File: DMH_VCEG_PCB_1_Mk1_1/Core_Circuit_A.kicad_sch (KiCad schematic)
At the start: 112 parts, among them J21 Conn_01x10_PinHeader, J22 Conn_01x10_PinHeader, J23 Conn_01x10_PinHeader, J24 Conn_01x06_PinHeader, Q1 BC558, Q10 BC548, Q2 BC558, Q3 BC548, Q4 BC548, Q5 BS170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

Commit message: Out R rework ongoing
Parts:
- removed Q5, Q6: BS170, Package_TO_SOT_THT:TO-92_Inline, symbol Transistor_FET:BS170
- R8: value 100k -> 150k
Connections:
- net +12V: now also Q2.3 (E), R1.1
- net -12V: no longer RV2.1, RV2.2
- net GND: no longer U7.12 (+)
- net InvGate: no longer R3.1
- net at R6.1: no longer RV2.3
- now unconnected: R3.2, R6.2, RV1.1, RV1.2, RV1.3, U7.13 (-), U7.14
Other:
- moved on the sheet: Q1, Q2, R1, R3, R6, R8, RV1, RV2, U7D

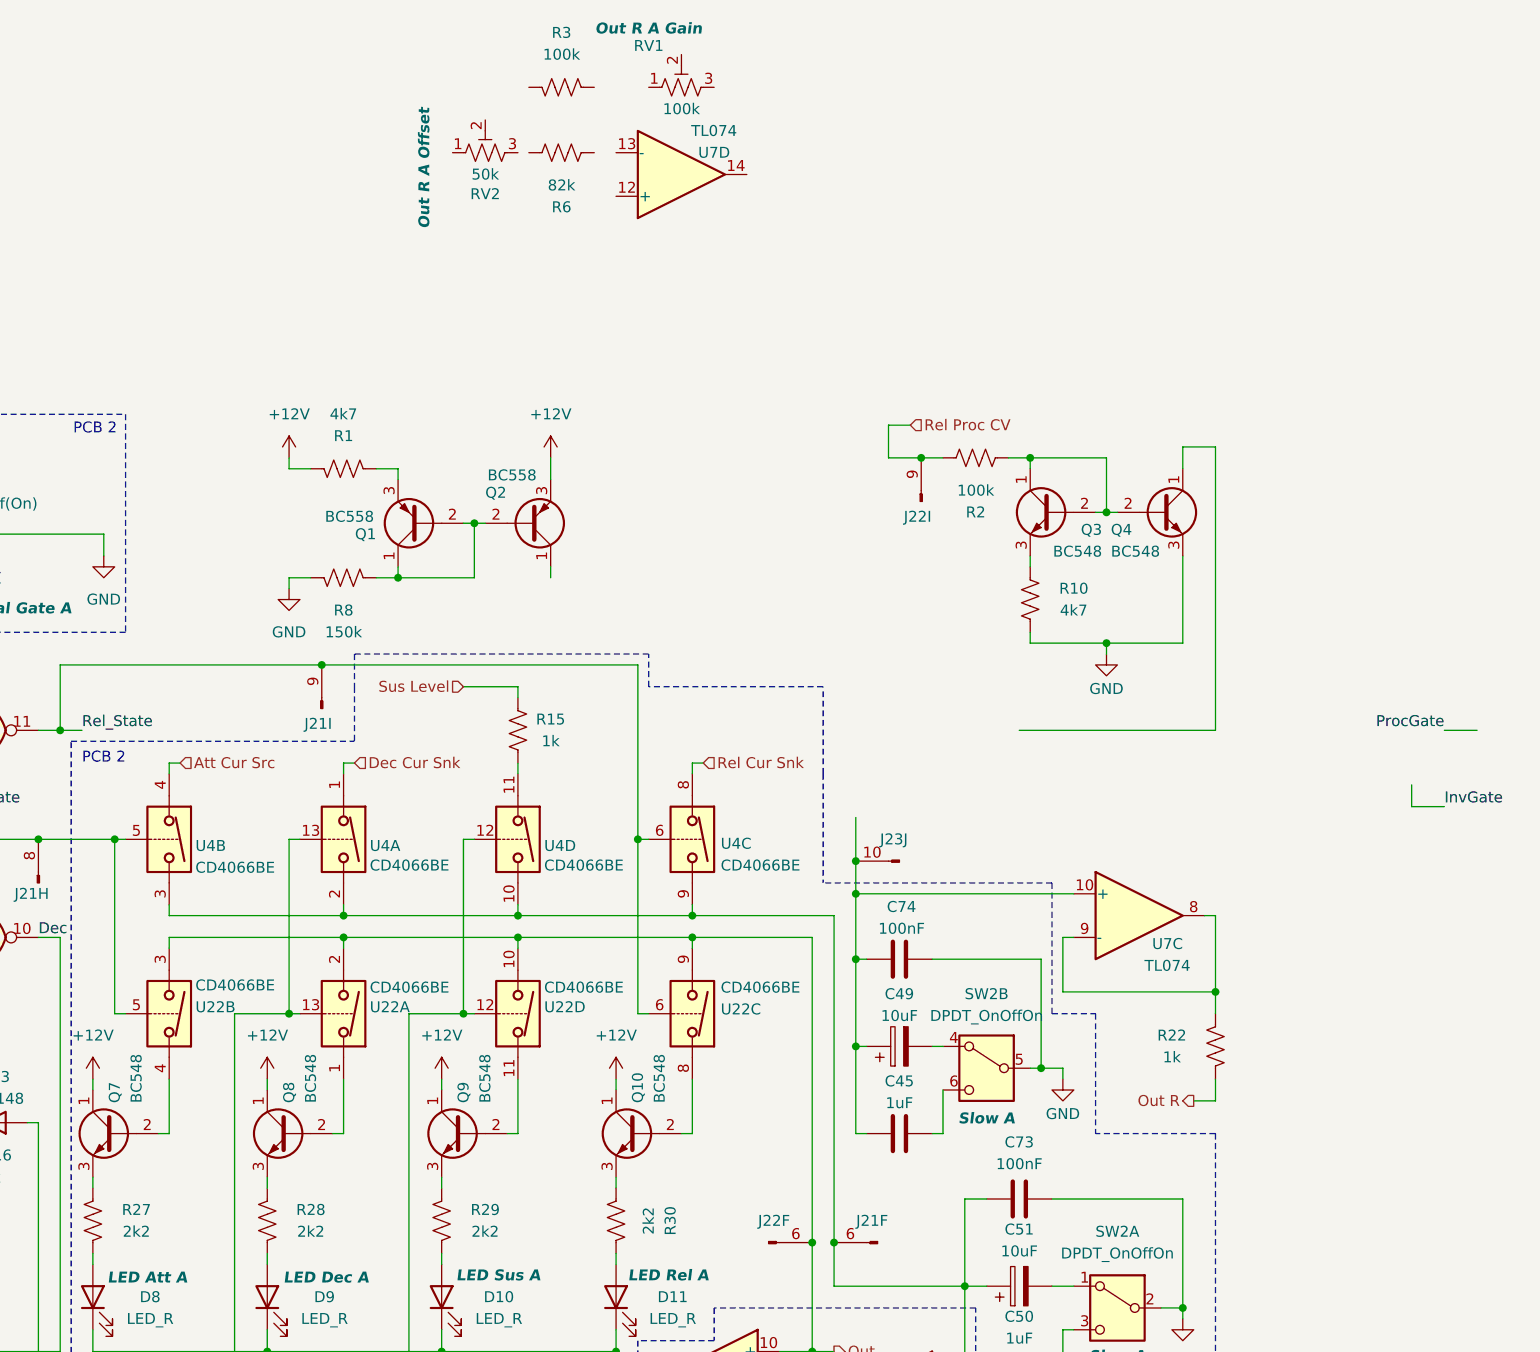
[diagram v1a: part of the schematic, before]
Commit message: Changed Out R design on Circuit A
Needs testing on breadboard
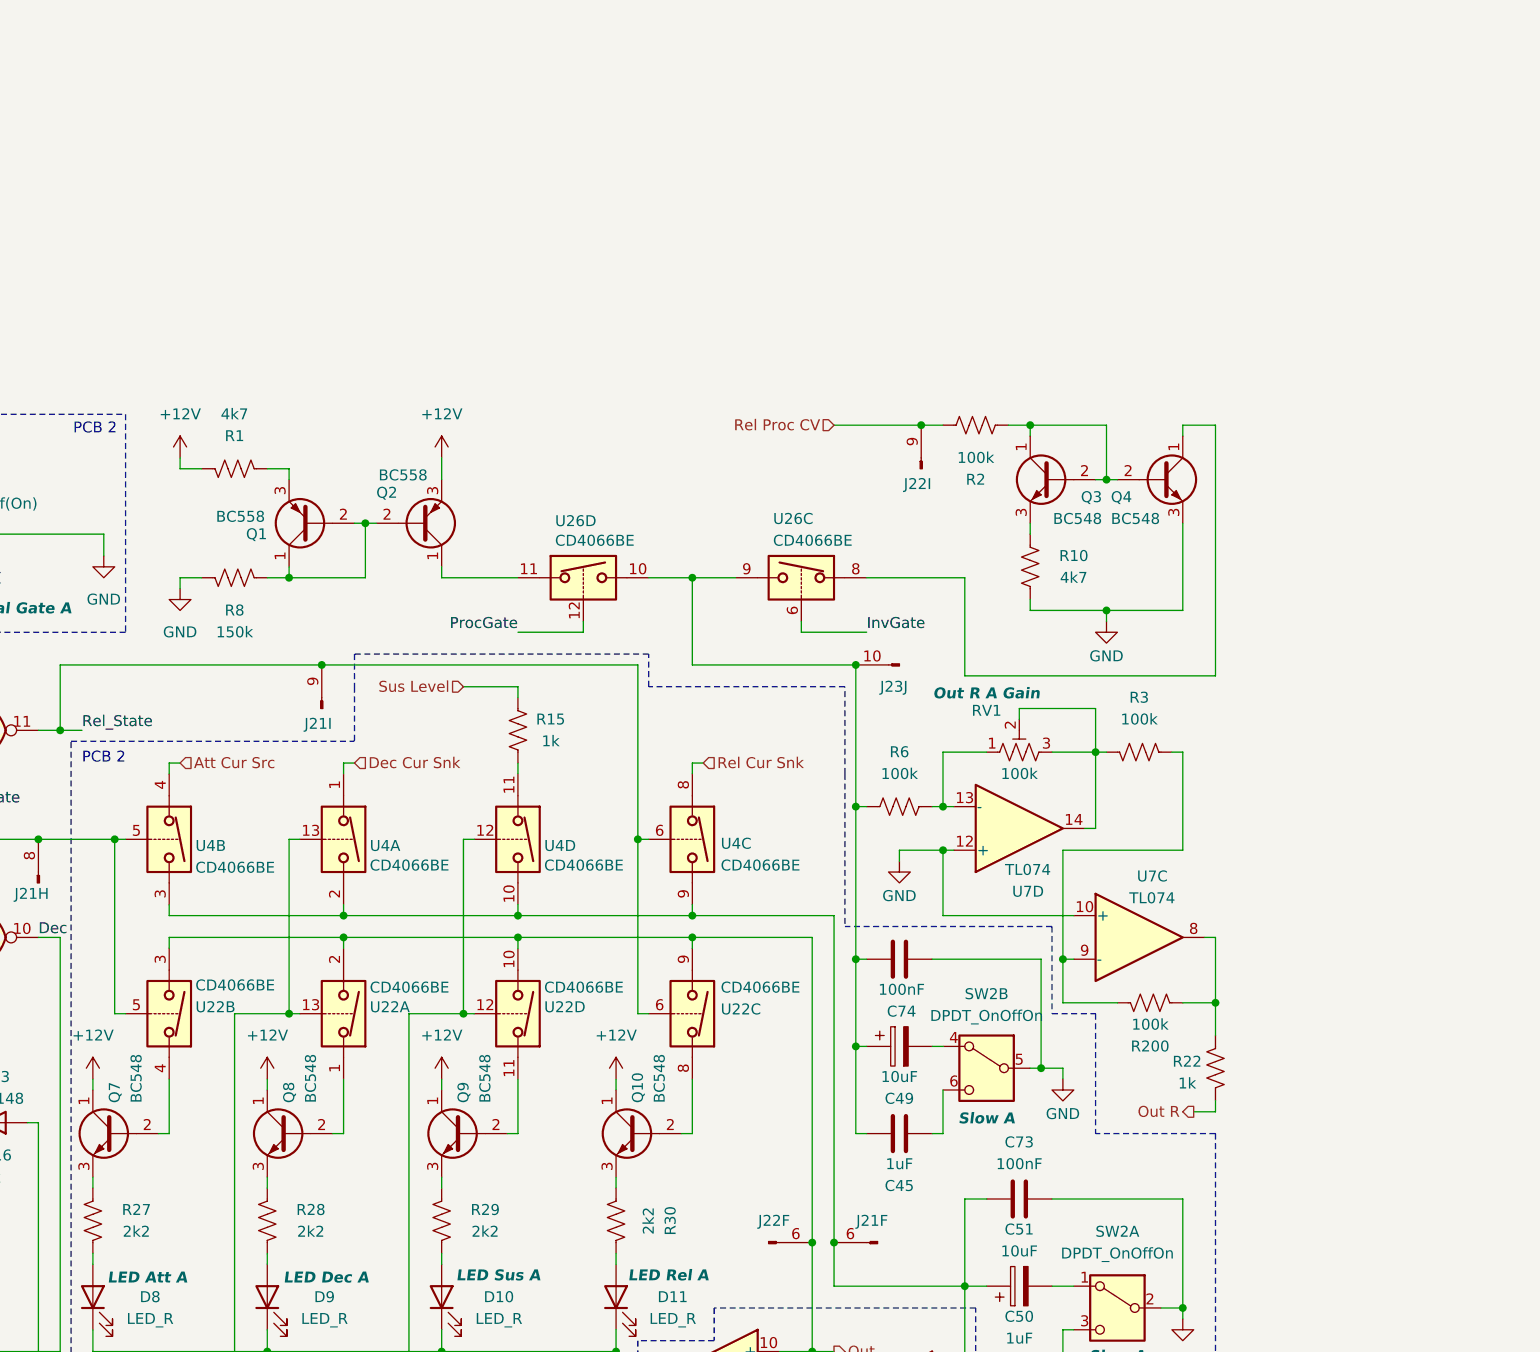
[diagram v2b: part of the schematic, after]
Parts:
- removed RV2: 50k, Potentiometer_THT:Potentiometer_Bourns_3296W_Vertical, symbol Device:R_Potentiometer_Trim_US
- added R200: 100k, Resistor_THT:R_Axial_DIN0207_L6.3mm_D2.5mm_P7.62mm_Horizontal, symbol Device:R_US
- added U26: CD4066BE, Package_DIP:DIP-14_W7.62mm, symbol Analog_Switch:CD4066BE
- R6: value 82k -> 100k
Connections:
- net GND: now also U7.10 (+), U7.12 (+)
- net InvGate: now also U26.6
- net ProcGate: now also U26.12
- net at C45.2, C49.1, C74.2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: now also R6.2, U26.10, U26.9; no longer U7.10 (+)
- net at R6.1: now also RV1.1, U7.13 (-)
- net at R3.1: now also RV1.2, RV1.3, U7.14
- net at R3.2: now also U7.9 (-), R200.2
- net at Q4.1 (C): now also U26.8
- net at R22.2, U7.8: now also R200.1; no longer U7.9 (-)
- net at Q2.1 (C): now also U26.11
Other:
- moved on the sheet: J22I, J23J, Q1, Q2, Q3, Q4, R1, R10, R2, R22, R3, R6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

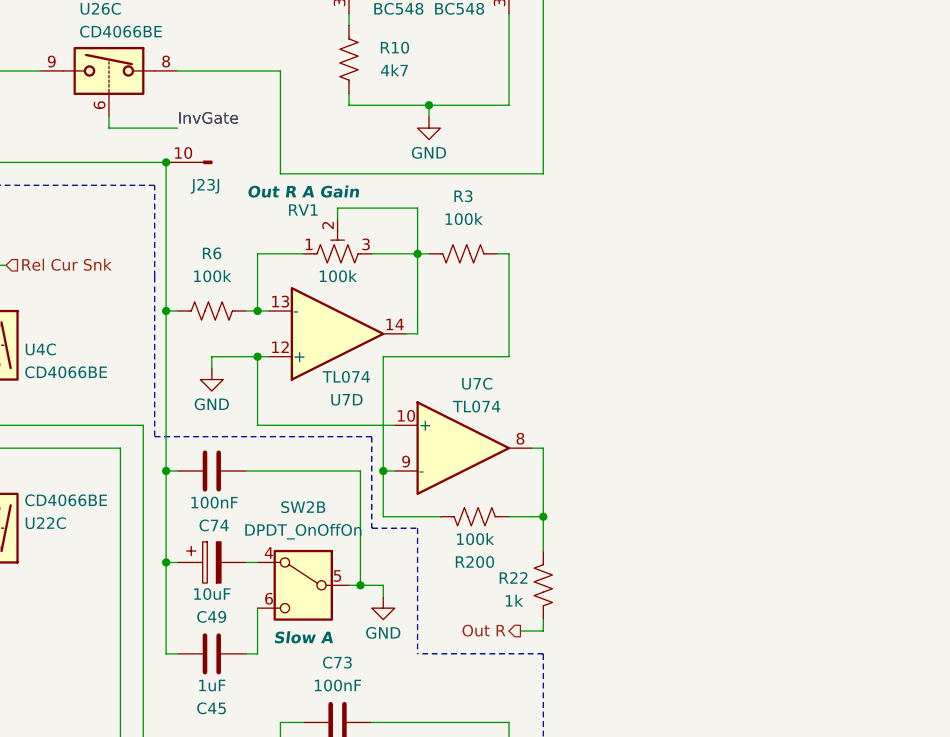
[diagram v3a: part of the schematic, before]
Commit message: Modified Out R output buffer
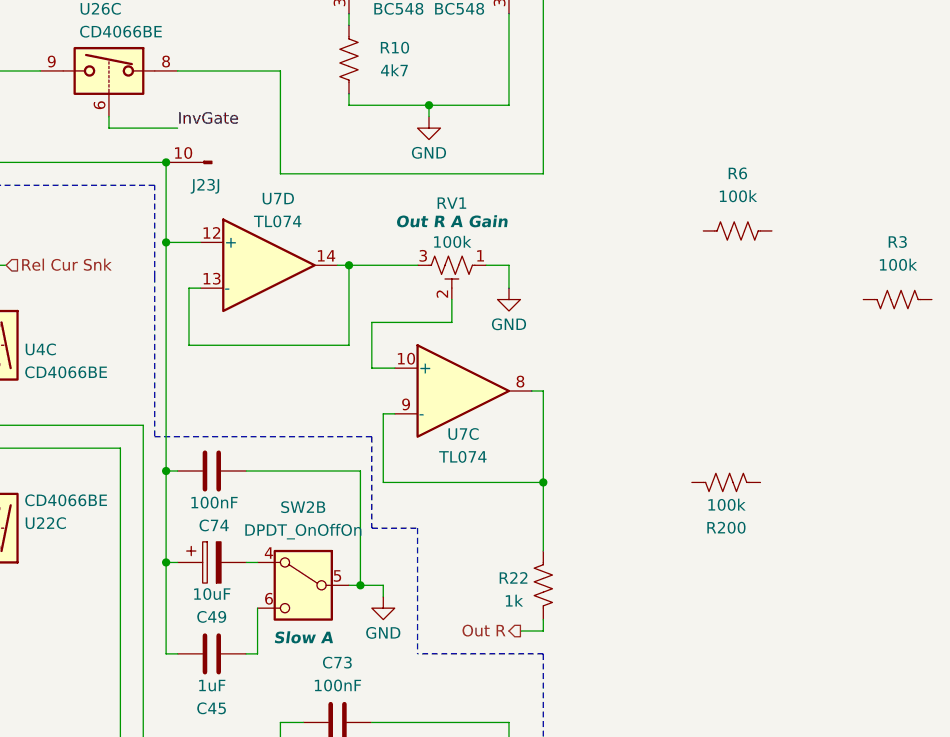
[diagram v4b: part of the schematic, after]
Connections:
- net GND: now also RV1.1; no longer U7.10 (+), U7.12 (+)
- net at C45.2, C49.1, C74.2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: now also U7.12 (+); no longer R6.2
- net at RV1.3, U7.14: now also U7.13 (-); no longer R3.1, RV1.2
- net at R22.2, U7.8: now also U7.9 (-); no longer R200.1
- new net: RV1.2, U7.10 (+)
- now unconnected: R200.2, R3.2, R6.1
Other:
- moved on the sheet: R200, R3, R6, RV1, U7C, U7D

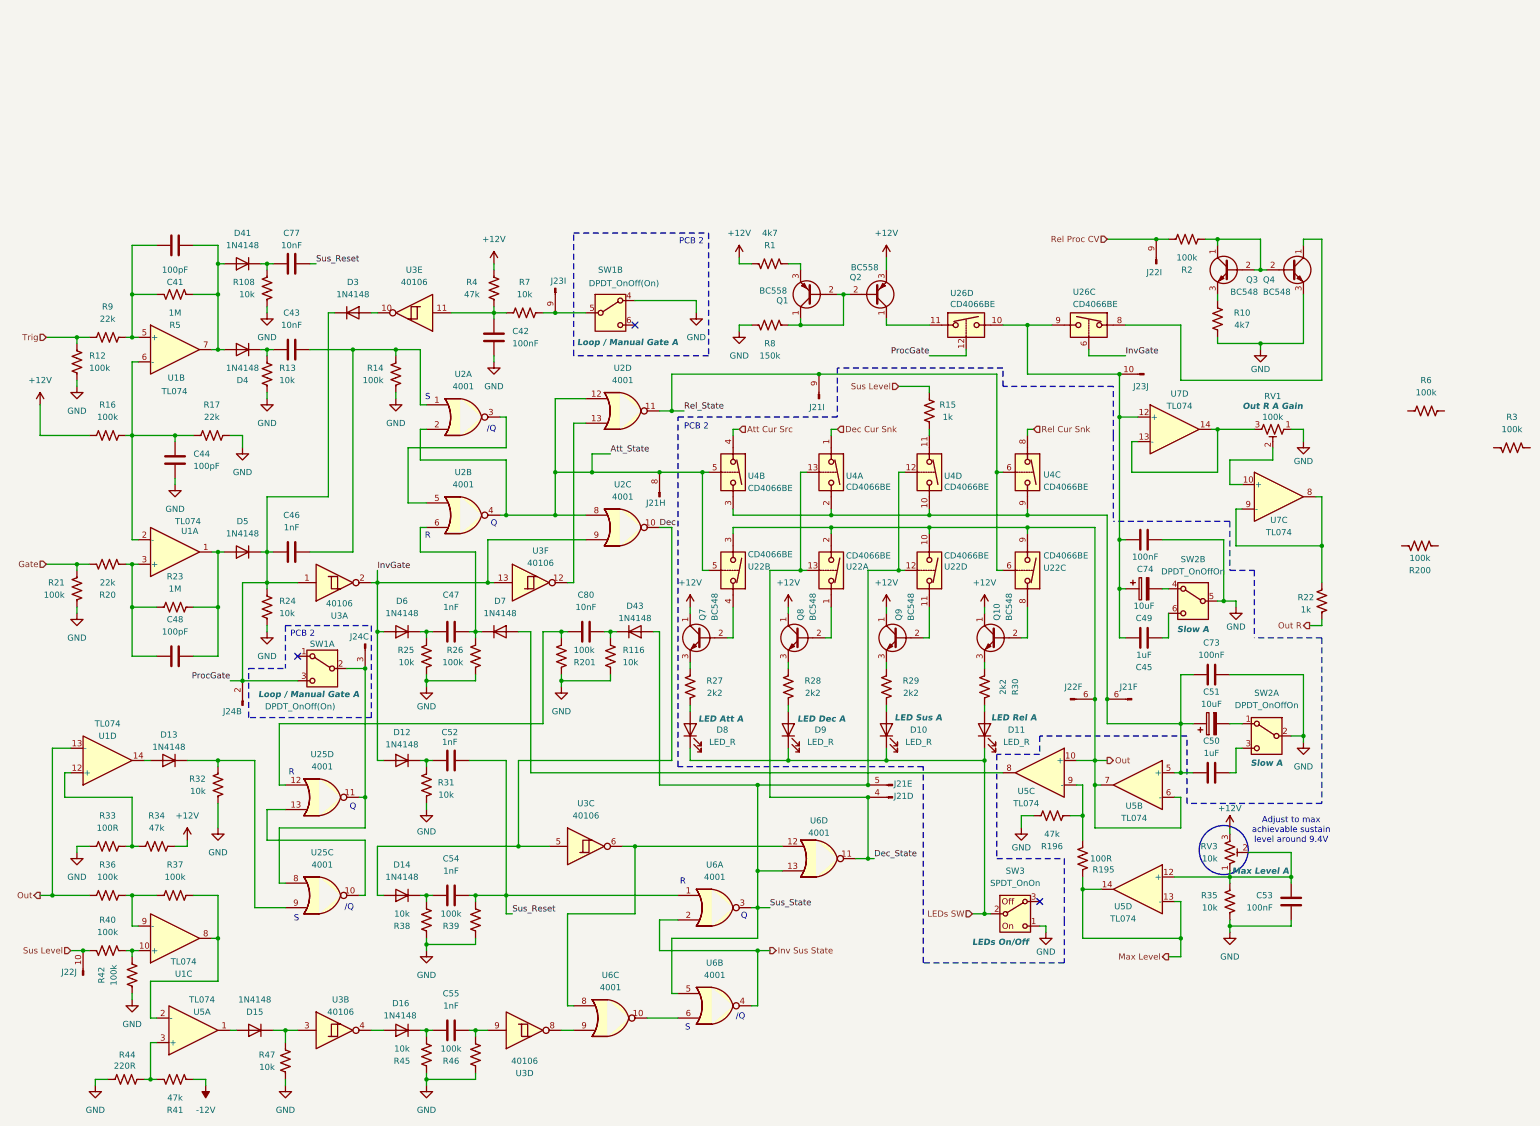
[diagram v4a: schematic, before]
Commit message: Validated Out R design
Next step is to update Circuit B with it and then respin PCB 1
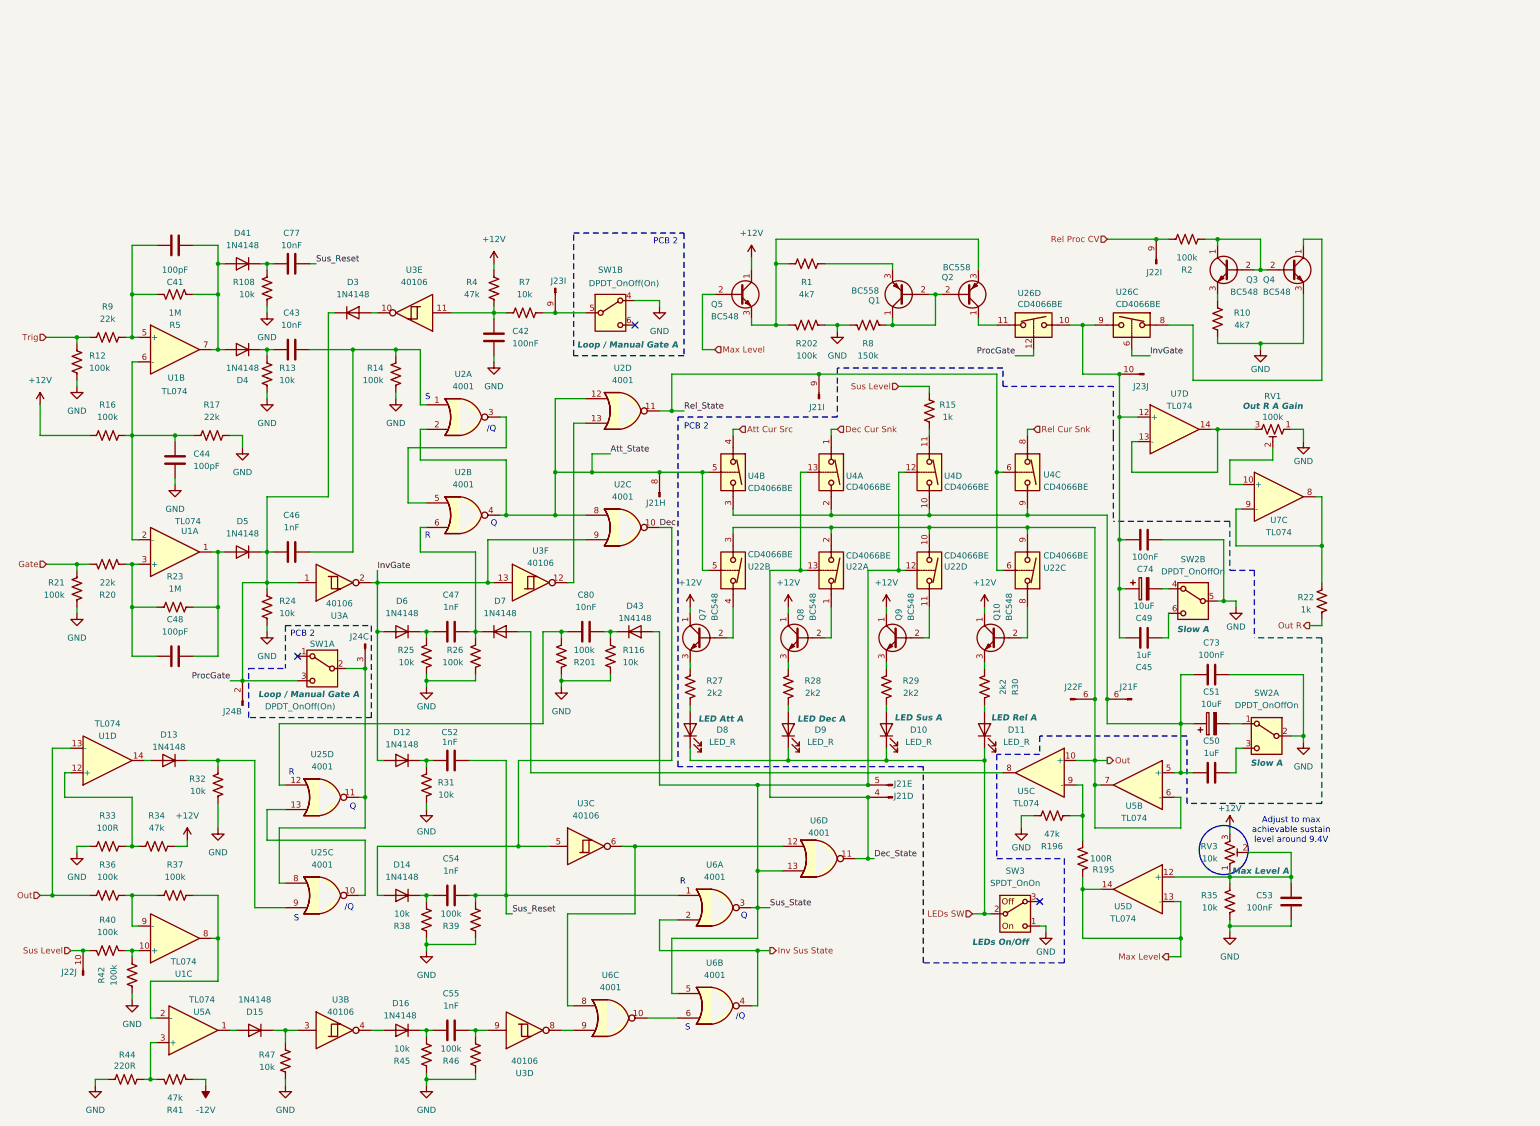
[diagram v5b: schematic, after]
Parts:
- removed R200, R3, R6: 100k, Resistor_THT:R_Axial_DIN0207_L6.3mm_D2.5mm_P7.62mm_Horizontal, symbol Device:R_US
- added Q5: BC548, Package_TO_SOT_THT:TO-92L_Inline_Wide, symbol Transistor_BJT:BC548
- added R202: 100k, Resistor_THT:R_Axial_DIN0207_L6.3mm_D2.5mm_P7.62mm_Horizontal, symbol Device:R_US
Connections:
- net +12V: now also Q5.1 (C); no longer Q2.3 (E), R1.1
- net GND: now also R202.1
- net Max Level: now also Q5.2 (B)
- new net: Q2.3 (E), Q5.3 (E), R1.1, R202.2
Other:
- moved on the sheet: Q1, Q2, R1, R8, U26C, U26D
